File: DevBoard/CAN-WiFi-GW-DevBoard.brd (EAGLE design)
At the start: 82.5 x 58.4 mm, 30 parts, among them SW1 CONFIGURATION, U1 74LVC1T45GW,125, U2 74LVC1T45GW,125, U3 74LVC1T45GW,125, X1 MKDSN1,5/2-5,08

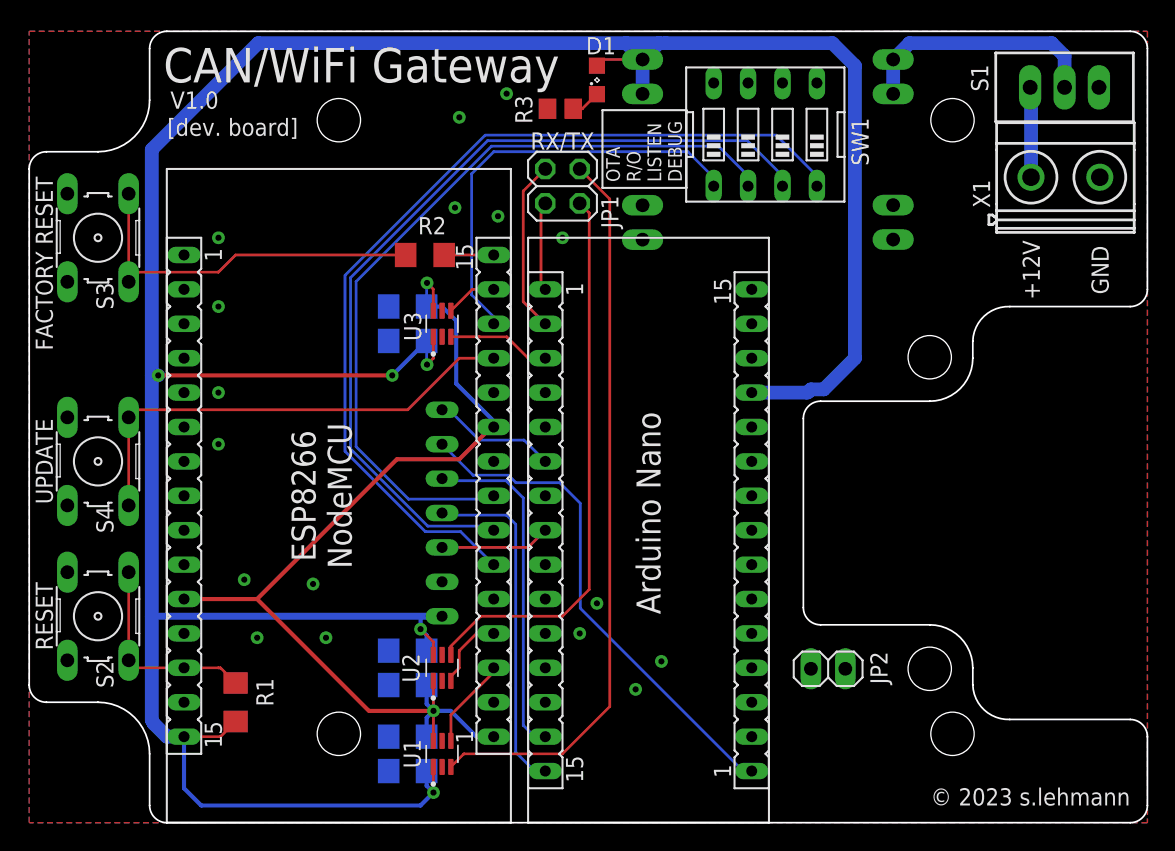
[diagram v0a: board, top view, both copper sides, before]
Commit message: Revision dev-board fixing button mistakes, physical dimensions and robustness.
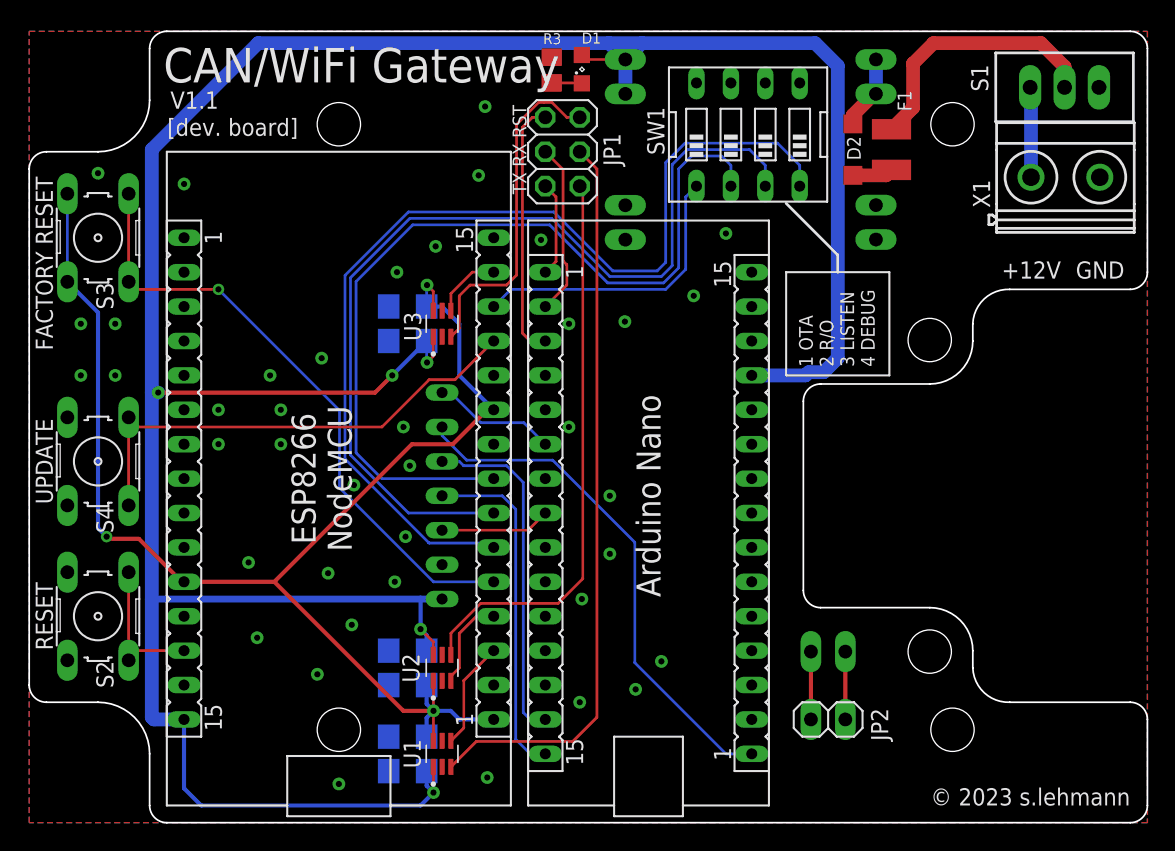
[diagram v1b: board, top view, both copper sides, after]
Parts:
- removed CAN_MODULE: (no value), con-lsta:FE07
- removed PWR_IN+, PWR_IN-, PWR_OUT+, PWR_OUT-: (no value), pinhead:1X02
- removed R1: 10k, rcl:R1206
- removed R2: 1k, rcl:R1206
- removed SV1, SV2, SV3, SV4: (no value), con-lsta:FE15
- added D2: MBR0520LT, diode:SOD123
- added F1: 500mA, custom:FSMD050-1210-R
- added J1: IN+, pinhead:1X02
- added J10, J7, J8, J9: (no value), con-lsta:FE15
- added J2: OUT+, pinhead:1X02
- added J3: IN-, pinhead:1X02
- added J4: OUT-, pinhead:1X02
- added J5: CAN_MODULE, con-lsta:FE07
- added J6: (no value), pinhead:1X02
- JP1: device pinhead:2X02 -> pinhead:2X03
- R3: value 150 -> 1k
- moved JP2 3.74 mm to (59.0, 7.62)
- moved R3 2.93 mm to (38.6, 55.6), turned to 270 degrees
- moved JP1 2.54 mm to (39.4, 49.5)
- moved D1 1.37 mm to (40.8, 55.6)
- moved SW1 1.27 mm to (53.1, 50.8)
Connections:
- removed net ESP_D0/FAC_RST: R2.1, SV2.15
- removed net FAC_RST: R2.2, S3.1, S3.2
- new net ESP_D8/FAC_RST: J8.5, S3.1, S3.2
- new net N$2: J6.1, JP2.1
- new net N$3: J6.2, JP2.2
- new net N$4: F1.1, S1.2
- new net N$5: D2.A, F1.2
- new net N$6: JP1.5, U3.3
- net +3V3: now also J7.11, J8.1, J8.10, S3.3, S3.4; no longer SV1.11, SV2.1, SV2.10
- net +5V: now also J10.12, J2.1, J2.2, J5.7, J7.15; no longer CAN_MODULE.7, PWR_OUT+.1, PWR_OUT+.2, R1.1, SV1.15, SV4.12
- net AR_RST: now also J9.3, JP1.6; no longer SV3.3, U3.3
- net AR_RX: now also J9.2; no longer SV3.2
- net AR_TX: now also J9.1; no longer SV3.1
- net CS: now also J5.5, J9.8; no longer CAN_MODULE.5, SV3.8
- net ESP_D1: now also J8.14; no longer SV2.14
- net ESP_D2/OTA_EN: now also J8.13; no longer SV2.13
- net ESP_D3/UPDATE: now also J8.12; no longer SV2.12
- net ESP_D5/WRITE_EN: now also J8.8; no longer SV2.8
- net ESP_D6/LISTEN_MODE: now also J8.7; no longer SV2.7
- net ESP_D7/DEBUG_MODE: now also J8.6; no longer SV2.6
- net ESP_RST: now also J7.13; no longer R1.2, SV1.13
- net ESP_RX: now also J8.4; no longer SV2.4
- net ESP_TX: now also J8.3; no longer SV2.3
- net GND: now also J10.14, J3.1, J3.2, J4.1, J4.2, J5.6, J7.10, J7.14, J8.2, J8.9, J9.4; no longer CAN_MODULE.6, PWR_IN-.1, PWR_IN-.2, PWR_OUT-.1, PWR_OUT-.2, S3.3, S3.4, SV1.10, SV1.14, SV2.2, SV2.9, SV3.4, SV4.14
- net INT: now also J5.1, J9.6; no longer CAN_MODULE.1, SV3.6
- net SCK: now also J10.1, J5.2; no longer CAN_MODULE.2, SV4.1
- net SI/MOSI: now also J5.3, J9.14; no longer CAN_MODULE.3, SV3.14
- net SO/MISO: now also J5.4, J9.15; no longer CAN_MODULE.4, SV3.15
- net VIN: now also D2.C, J1.1, J1.2; no longer PWR_IN+.1, PWR_IN+.2, S1.2
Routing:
- net ESP_D8/FAC_RST: track 0.00 -> 46.0 mm, vias 0 -> 1
- net +3V3: track 74.1 -> 104.8 mm, vias 2 -> 3
- net FAC_RST: track 27.8 -> 0.00 mm
- net N$6: track 0.00 -> 25.1 mm
- net N$4: track 0.00 -> 19.6 mm
- net VIN: track 18.4 -> 5.54 mm
- net AR_RST: track 7.62 -> 19.1 mm
- net ESP_D2/OTA_EN: track 31.7 -> 21.8 mm
- net ESP_D7/DEBUG_MODE: track 68.6 -> 75.0 mm
- net ESP_D6/LISTEN_MODE: track 63.6 -> 69.9 mm
- net ESP_D5/WRITE_EN: track 58.8 -> 64.8 mm
- net +5V: track 223.6 -> 218.1 mm
- net N$3: track 0.00 -> 5.01 mm
- net N$2: track 0.00 -> 5.01 mm
- net ESP_RST: track 15.1 -> 10.9 mm
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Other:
- outline, holes or cut-outs redrawn
- board text added: "1 OTA 2 R/O 3 LISTEN 4 DEBUG"
- board text added: "TX RX RST"
- board text added: "V1.1"
- board text removed: "IN+"
- board text removed: "IN-"
- board text removed: "OTA R/O LISTEN DEBUG"
- board text removed: "OUT+"
- board text removed: "OUT-"
- board text removed: "RX/TX"
- board text removed: "V1.0"
